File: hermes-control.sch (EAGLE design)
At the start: 71 parts, among them J3 2201778-1, Q1 MMBT2222A, Q2 BC849SMD, Q3 FDN360P, Q4 FDN360P, Q5 BC849SMD, Q6 MMBT2222A, Q7 FDN360P, U1 LSM9DS1TR, U2 ESP32-WROOM-32D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

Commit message: addressed more reviews
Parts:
- C15: value 100uF -> 100nF
- C9: value 10uF -> 10nF 16v
- R7: value 100k -> 100k 1%
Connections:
- removed net N$15: R6.1, U$2.2
- removed net N$16: C13.1, U1.VDDIO
- new net PROBE: R6.1, U$2.2, U2.IO33
- net 3.3V: now also C13.1, U1.VDDIO
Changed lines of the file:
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@@
 <part name="R20" library="rcl" library_urn="urn:adsk.eagle:library:334" deviceset="R-US_" device="R0603" package3d_urn="urn:adsk.eagle:package:23555/3" value="10k"/>
 <part name="R23" library="rcl" library_urn="urn:adsk.eagle:library:334" deviceset="R-US_" device="R0603" package3d_urn="urn:adsk.eagle:package:23555/3" value="33k"/>
-<part name="R7" library="rcl" library_urn="urn:adsk.eagle:library:334" deviceset="R-US_" device="R0603" package3d_urn="urn:adsk.eagle:package:23555/3" value="100k"/>
+<part name="R7" library="rcl" library_urn="urn:adsk.eagle:library:334" deviceset="R-US_" device="R0603" package3d_urn="urn:adsk.eagle:package:23555/3" value="100k 1%"/>
 <part name="R8" library="rcl" library_urn="urn:adsk.eagle:library:334" deviceset="R-US_" device="R0603" package3d_urn="urn:adsk.eagle:package:23555/3" value="10k"/>
 <part name="R9" library="rcl" library_urn="urn:adsk.eagle:library:334" deviceset="R-US_" device="R0603" package3d_urn="urn:adsk.eagle:package:23555/3" value="10k"/>
@@
 <part name="SUPPLY27" library="SparkFun-PowerSymbols" library_urn="urn:adsk.eagle:library:530" deviceset="VCC" device=""/>
 <part name="SUPPLY28" library="SparkFun-PowerSymbols" library_urn="urn:adsk.eagle:library:530" deviceset="3.3V" device=""/>
-<part name="C9" library="rcl" library_urn="urn:adsk.eagle:library:334" deviceset="C-US" device="C0603" package3d_urn="urn:adsk.eagle:package:23616/2" value="10uF"/>
-<part name="C15" library="rcl" library_urn="urn:adsk.eagle:library:334" deviceset="C-US" device="C0603" package3d_urn="urn:adsk.eagle:package:23616/2" value="100uF"/>
+<part name="C9" library="rcl" library_urn="urn:adsk.eagle:library:334" deviceset="C-US" device="C0603" package3d_urn="urn:adsk.eagle:package:23616/2" value="10nF 16v"/>
+<part name="C15" library="rcl" library_urn="urn:adsk.eagle:library:334" deviceset="C-US" device="C0603" package3d_urn="urn:adsk.eagle:package:23616/2" value="100nF"/>
 <part name="R4" library="rcl" library_urn="urn:adsk.eagle:library:334" deviceset="R-US_" device="R0603" package3d_urn="urn:adsk.eagle:package:23555/3" value="1k"/>
 <part name="R16" library="rcl" library_urn="urn:adsk.eagle:library:334" deviceset="R-US_" device="R0603" package3d_urn="urn:adsk.eagle:package:23555/3" value="1k"/>
@@
 <attribute name="VALUE" x="111.76" y="53.34" size="1.778" layer="96"/>
 </instance>
-<instance part="U$2" gate="G$1" x="83.82" y="83.82" smashed="yes" rot="R180"/>
-<instance part="GND29" gate="1" x="88.9" y="68.58" smashed="yes">
-<attribute name="VALUE" x="86.36" y="66.04" size="1.778" layer="96"/>
-</instance>
-<instance part="SUPPLY27" gate="G$1" x="88.9" y="86.36" smashed="yes">
-<attribute name="VALUE" x="88.9" y="89.154" size="1.778" layer="96" align="bottom-center"/>
+<instance part="U$2" gate="G$1" x="81.28" y="83.82" smashed="yes" rot="R180"/>
+<instance part="GND29" gate="1" x="86.36" y="68.58" smashed="yes">
+<attribute name="VALUE" x="83.82" y="66.04" size="1.778" layer="96"/>
+</instance>
+<instance part="SUPPLY27" gate="G$1" x="86.36" y="86.36" smashed="yes">
+<attribute name="VALUE" x="86.36" y="89.154" size="1.778" layer="96" align="bottom-center"/>
 </instance>
 <instance part="SUPPLY28" gate="G$1" x="200.66" y="134.62" smashed="yes">
@@
 <pinref part="GND29" gate="1" pin="GND"/>
 <pinref part="U$2" gate="G$1" pin="3"/>
-<wire x1="88.9" y1="71.12" x2="88.9" y2="76.2" width="0.1524" layer="91"/>
+<wire x1="86.36" y1="71.12" x2="86.36" y2="76.2" width="0.1524" layer="91"/>
 </segment>
 </net>
@@
 <pinref part="U$2" gate="G$1" pin="1"/>
 <pinref part="SUPPLY27" gate="G$1" pin="VCC"/>
-<wire x1="88.9" y1="81.28" x2="88.9" y2="86.36" width="0.1524" layer="91"/>
+<wire x1="86.36" y1="81.28" x2="86.36" y2="86.36" width="0.1524" layer="91"/>
 </segment>
 </net>
@@
 <pinref part="U1" gate="G$1" pin="VDD"/>
 <wire x1="411.48" y1="142.24" x2="414.02" y2="142.24" width="0.1524" layer="91"/>
-<wire x1="414.02" y1="142.24" x2="414.02" y2="160.02" width="0.1524" layer="91"/>
+<wire x1="414.02" y1="142.24" x2="414.02" y2="144.78" width="0.1524" layer="91"/>
+<wire x1="414.02" y1="144.78" x2="414.02" y2="160.02" width="0.1524" layer="91"/>
 <wire x1="391.16" y1="160.02" x2="403.86" y2="160.02" width="0.1524" layer="91"/>
 <pinref part="SUPPLY24" gate="G$1" pin="3.3V"/>
@@
 <pinref part="C12" gate="G$1" pin="1"/>
 <junction x="403.86" y="160.02"/>
+<pinref part="U1" gate="G$1" pin="VDDIO"/>
+<wire x1="411.48" y1="139.7" x2="419.1" y2="139.7" width="0.1524" layer="91"/>
+<wire x1="419.1" y1="139.7" x2="419.1" y2="144.78" width="0.1524" layer="91"/>
+<wire x1="419.1" y1="144.78" x2="426.72" y2="144.78" width="0.1524" layer="91"/>
+<pinref part="C13" gate="G$1" pin="1"/>
+<wire x1="419.1" y1="144.78" x2="414.02" y2="144.78" width="0.1524" layer="91"/>
+<junction x="419.1" y="144.78"/>
+<junction x="414.02" y="144.78"/>
 </segment>
 <segment>
@@
 </segment>
 </net>
-<net name="N$16" class="0">
-<segment>
-<pinref part="U1" gate="G$1" pin="VDDIO"/>
-<wire x1="411.48" y1="139.7" x2="419.1" y2="139.7" width="0.1524" layer="91"/>
-<wire x1="419.1" y1="139.7" x2="419.1" y2="144.78" width="0.1524" layer="91"/>
-<wire x1="419.1" y1="144.78" x2="426.72" y2="144.78" width="0.1524" layer="91"/>
-<pinref part="C13" gate="G$1" pin="1"/>
-</segment>
-</net>
 <net name="DTR" class="0">
 <segment>
@@
 <pinref part="Q6" gate="&gt;NAME" pin="C"/>
 <wire x1="114.3" y1="86.36" x2="114.3" y2="83.82" width="0.1524" layer="91"/>
-</segment>
-</net>
-<net name="N$15" class="0">
-<segment>
-<pinref part="U$2" gate="G$1" pin="2"/>
-<pinref part="R6" gate="G$1" pin="1"/>
-<wire x1="88.9" y1="78.74" x2="93.98" y2="78.74" width="0.1524" layer="91"/>
 </segment>
 </net>
@@
 </segment>
 </net>
+<net name="PROBE" class="0">
+<segment>
+<pinref part="U2" gate="G$1" pin="IO33"/>
+<wire x1="312.42" y1="88.9" x2="320.04" y2="88.9" width="0.1524" layer="91"/>
+<label x="314.96" y="88.9" size="1.778" layer="95"/>
+</segment>
+<segment>
+<pinref part="U$2" gate="G$1" pin="2"/>
+<pinref part="R6" gate="G$1" pin="1"/>
+<wire x1="86.36" y1="78.74" x2="93.98" y2="78.74" width="0.1524" layer="91"/>
+<label x="86.36" y="78.74" size="1.778" layer="95"/>
+</segment>
+</net>

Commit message: added two more i2c connections
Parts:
- removed U$6: JST-GH-4TOP, BlueRobotics-JST-GH:JST-GH-4TOP
- added U$10, U$11, U$9: JST-GH-4TOP, BlueRobotics-JST-GH:JST-GH-4TOP
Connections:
- net 3.3V: now also Q7.D, U$10.1, U$11.1, U$9.1; no longer Q7.S, U$6.1
- net GND: now also U$10.4, U$11.4, U$9.4; no longer U$6.4
- net SCL: now also U$10.2, U$11.2, U$9.2; no longer U$6.2
- net SDA: now also U$10.3, U$11.3, U$9.3; no longer U$6.3
- net VCCIO: now also Q7.S; no longer Q7.D
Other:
- moved on the sheet: Q7

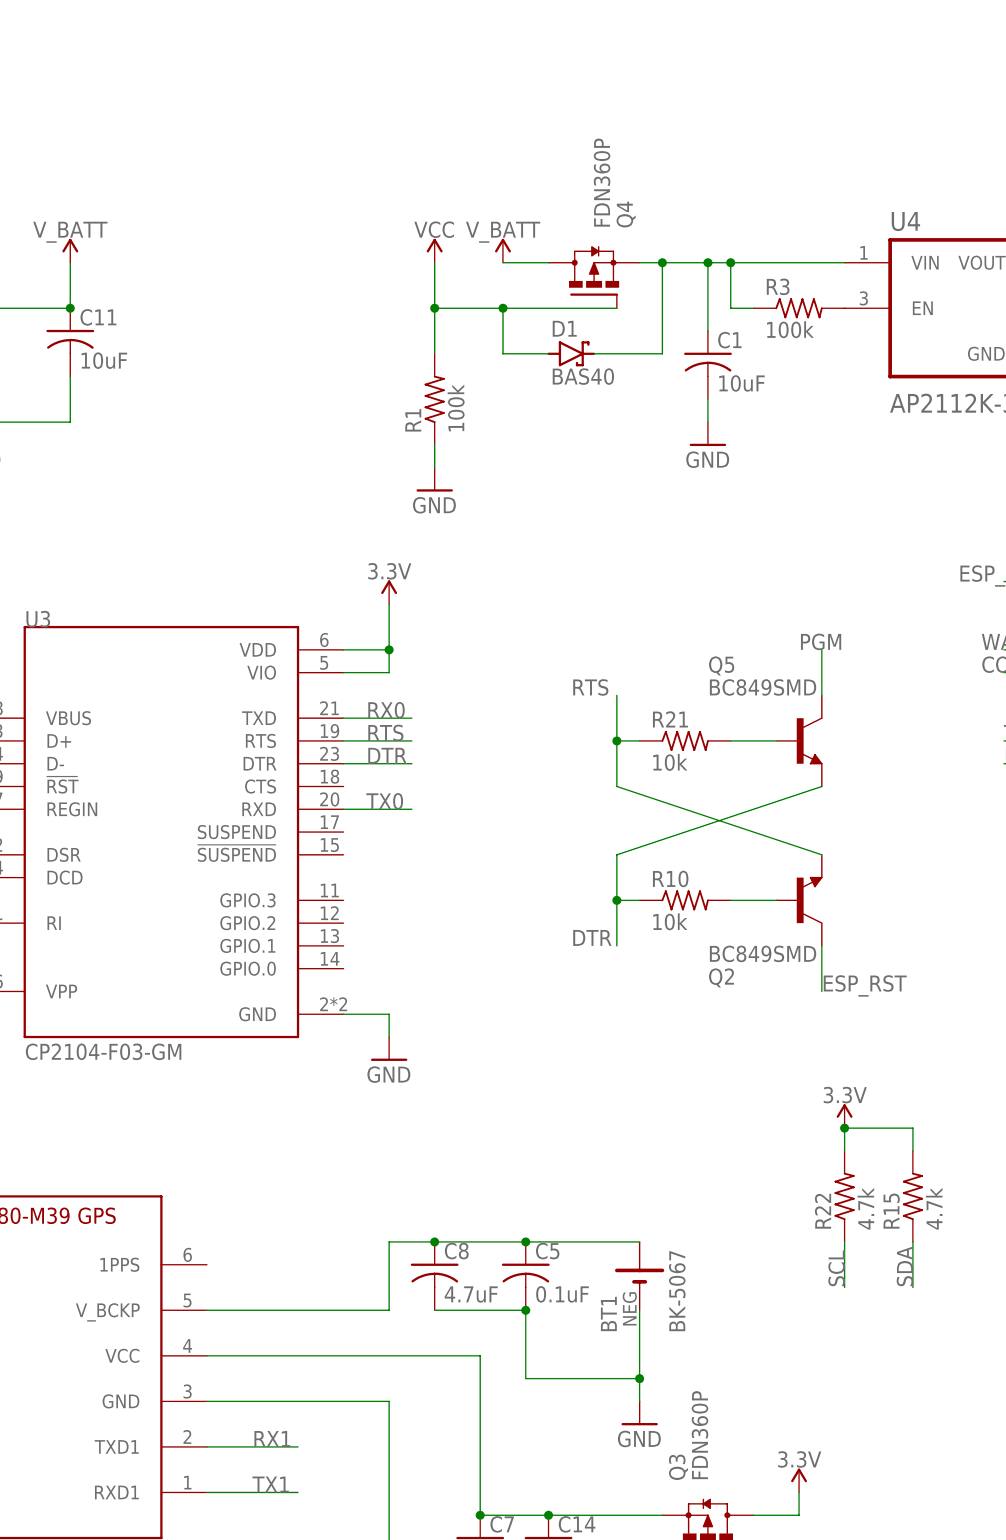
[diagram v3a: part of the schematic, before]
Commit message: new layout with main componets
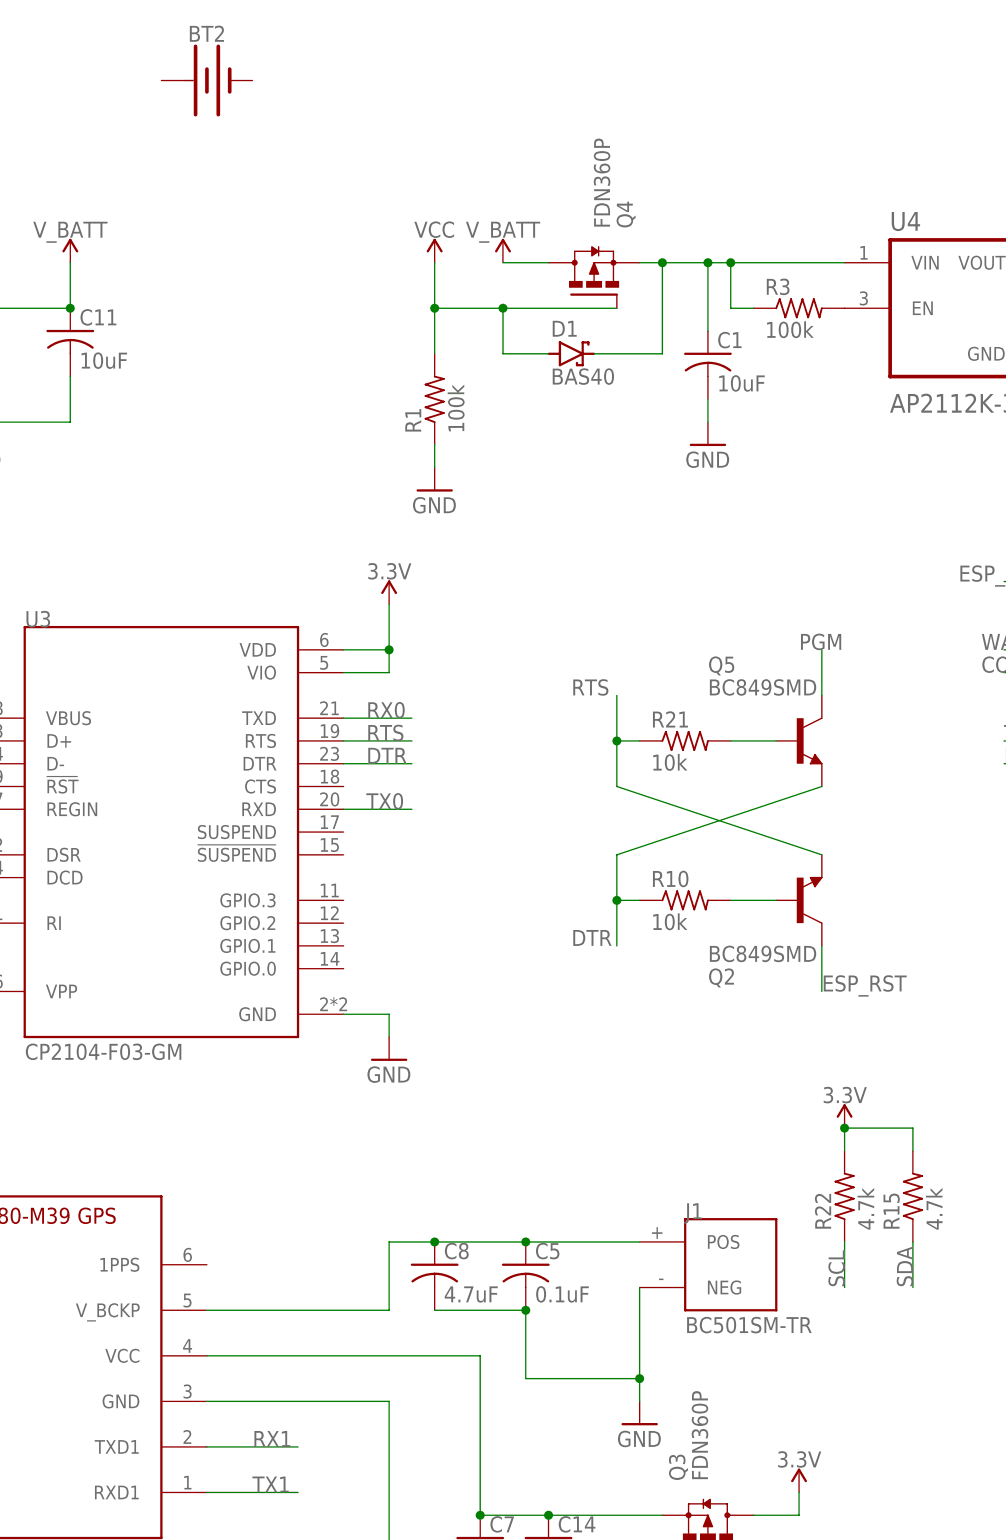
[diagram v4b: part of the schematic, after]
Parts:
- removed BT1: BK-5067, hermes:BK-5067
- added BT2: (no value), SparkFun-Batteries:BATTERY-18650
- added J1: BC501SM-TR, BC501SM-TR:BC501SM-TR
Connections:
- net GND: now also J1.NEG; no longer BT1.N
- net N$7: now also J1.POS; no longer BT1.P
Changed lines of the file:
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@@
 <?xml version="1.0" encoding="utf-8"?>
 <!DOCTYPE eagle SYSTEM "eagle.dtd">
-<eagle version="9.1.0">
+<eagle version="9.4.0">
 <drawing>
 <settings>
-<setting alwaysvectorfont="yes"/>
+<setting alwaysvectorfont="no"/>
 <setting verticaltext="up"/>
 </settings>
@@
 <part name="SUPPLY13" library="SparkFun-PowerSymbols" library_urn="urn:adsk.eagle:library:530" deviceset="V_BATT" device=""/>
 <part name="GND14" library="supply1" library_urn="urn:adsk.eagle:library:371" deviceset="GND" device=""/>
-<part name="S1" library="hermes" deviceset="1825910-7" device=""/>
 <part name="SUPPLY14" library="SparkFun-PowerSymbols" library_urn="urn:adsk.eagle:library:530" deviceset="3.3V" device=""/>
 <part name="GND15" library="supply1" library_urn="urn:adsk.eagle:library:371" deviceset="GND" device=""/>
@@
 <part name="GND13" library="supply1" library_urn="urn:adsk.eagle:library:371" deviceset="GND" device=""/>
 <part name="LBAT" library="hermes" deviceset="S2B-PH-SM4-TB(LF)(SN)" device=""/>
-<part name="BT1" library="hermes" deviceset="BK-5067" device=""/>
 <part name="S2" library="hermes" deviceset="1825910-7" device=""/>
 <part name="SUPPLY22" library="SparkFun-PowerSymbols" library_urn="urn:adsk.eagle:library:530" deviceset="3.3V" device=""/>
@@
 <part name="SUPPLY25" library="SparkFun-PowerSymbols" library_urn="urn:adsk.eagle:library:530" deviceset="3.3V" device=""/>
 <part name="SUPPLY29" library="SparkFun-PowerSymbols" library_urn="urn:adsk.eagle:library:530" deviceset="3.3V" device=""/>
+<part name="BT2" library="SparkFun-Batteries" library_urn="urn:adsk.eagle:library:508" deviceset="BATTERY" device="-18650" package3d_urn="urn:adsk.eagle:package:37227/1"/>
+<part name="J1" library="BC501SM-TR" deviceset="BC501SM-TR" device=""/>
+<part name="S1" library="hermes" deviceset="1825910-7" device=""/>
 </parts>
 <sheets>
@@
 <attribute name="VALUE" x="335.28" y="68.58" size="1.778" layer="96"/>
 </instance>
-<instance part="S1" gate="G$1" x="403.86" y="73.66" smashed="yes">
-<attribute name="NAME" x="403.86" y="75.184" size="1.778" layer="95" font="vector" align="bottom-center"/>
-</instance>
 <instance part="SUPPLY14" gate="G$1" x="421.64" y="66.04" smashed="yes">
 <attribute name="VALUE" x="421.64" y="68.834" size="1.778" layer="96" align="bottom-center"/>
@@
 <attribute name="VALUE" x="60.22268125" y="167.63188125" size="1.275409375" layer="96" rot="R90"/>
 </instance>
-<instance part="BT1" gate="G$1" x="228.6" y="60.96" smashed="yes" rot="R90">
-<attribute name="NAME" x="226.05975" y="53.33963125" size="1.778090625" layer="95" rot="R90"/>
-<attribute name="VALUE" x="233.68596875" y="53.331040625" size="1.780090625" layer="96" rot="R90"/>
-</instance>
 <instance part="S2" gate="G$1" x="403.86" y="58.42" smashed="yes">
 <attribute name="NAME" x="403.86" y="59.944" size="1.778" layer="95" font="vector" align="bottom-center"/>
@@
 <instance part="SUPPLY29" gate="G$1" x="43.18" y="104.14" smashed="yes">
 <attribute name="VALUE" x="43.18" y="106.934" size="1.778" layer="96" align="bottom-center"/>
+</instance>
+<instance part="BT2" gate="G$1" x="180.34" y="193.04" smashed="yes">
+<attribute name="NAME" x="180.34" y="197.358" size="1.778" layer="95" font="vector" align="bottom-center"/>
+<attribute name="VALUE" x="180.34" y="188.722" size="1.778" layer="96" font="vector" align="top-center"/>
+</instance>
+<instance part="J1" gate="G$1" x="238.76" y="60.96" smashed="yes">
+<attribute name="NAME" x="233.68" y="66.04" size="1.778" layer="95"/>
+<attribute name="VALUE" x="233.68" y="53.34" size="1.778" layer="96"/>
+</instance>
+<instance part="S1" gate="G$1" x="403.86" y="73.66" smashed="yes">
+<attribute name="NAME" x="403.86" y="75.184" size="1.778" layer="95" font="vector" align="bottom-center"/>
 </instance>
 </instances>
@@
 <pinref part="GND9" gate="1" pin="GND"/>
 <wire x1="228.6" y1="45.72" x2="228.6" y2="48.26" width="0.1524" layer="91"/>
-<wire x1="228.6" y1="48.26" x2="228.6" y2="55.88" width="0.1524" layer="91"/>
+<wire x1="228.6" y1="48.26" x2="228.6" y2="58.42" width="0.1524" layer="91"/>
 <wire x1="215.9" y1="55.88" x2="215.9" y2="48.26" width="0.1524" layer="91"/>
 <wire x1="215.9" y1="48.26" x2="228.6" y2="48.26" width="0.1524" layer="91"/>
 <junction x="228.6" y="48.26"/>
 <wire x1="205.74" y1="55.88" x2="215.9" y2="55.88" width="0.1524" layer="91"/>
-<pinref part="BT1" gate="G$1" pin="N"/>
 <pinref part="C5" gate="G$1" pin="2"/>
 <junction x="215.9" y="55.88"/>
 <pinref part="C8" gate="G$1" pin="2"/>
+<pinref part="J1" gate="G$1" pin="NEG"/>
 </segment>
 <segment>
@@
 <wire x1="421.64" y1="66.04" x2="416.56" y2="66.04" width="0.1524" layer="91"/>
 <wire x1="416.56" y1="66.04" x2="416.56" y2="71.12" width="0.1524" layer="91"/>
-<pinref part="S1" gate="G$1" pin="4"/>
 <wire x1="416.56" y1="71.12" x2="414.02" y2="71.12" width="0.1524" layer="91"/>
 <wire x1="416.56" y1="66.04" x2="416.56" y2="60.96" width="0.1524" layer="91"/>
@@
 <pinref part="S2" gate="G$1" pin="3"/>
 <wire x1="416.56" y1="60.96" x2="414.02" y2="60.96" width="0.1524" layer="91"/>
+<pinref part="S1" gate="G$1" pin="4"/>
 </segment>
 <segment>
@@
 <pinref part="U$1" gate="G$1" pin="V_BCKP"/>
 <wire x1="200.66" y1="55.88" x2="180.34" y2="55.88" width="0.1524" layer="91"/>
-<pinref part="BT1" gate="G$1" pin="P"/>
 <pinref part="C5" gate="G$1" pin="1"/>
 <junction x="215.9" y="63.5"/>
 <pinref part="C8" gate="G$1" pin="1"/>
 <junction x="205.74" y="63.5"/>
+<pinref part="J1" gate="G$1" pin="POS"/>
 </segment>
 </net>
@@
 <net name="CONFIG" class="0">
 <segment>
-<pinref part="S1" gate="G$1" pin="1"/>
 <wire x1="393.7" y1="76.2" x2="386.08" y2="76.2" width="0.1524" layer="91"/>
 <label x="383.54" y="76.2" size="1.778" layer="95"/>
 <pinref part="R8" gate="G$1" pin="2"/>
-</segment>
-<segment>
+<pinref part="S1" gate="G$1" pin="1"/>
+</segment>
+<segment>

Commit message: all componets placed
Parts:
- removed J2: (no value), SparkFun-Connectors:USB_MICRO-B_FEMALE-SMT
- removed S3: 1825910-7, hermes:1825910-7
- added BT1: 6.8MM_COIN_CELL, SparkFun-Batteries:BATTERY-6.8MM_SMD
- added D2: BAS40, diode:BAS40
- added Q8: MMBT2222A, hermes:MMBT2222A
- added R19: 1k, rcl:R-US_R0603
- added R25: 4.7k, rcl:R-US_R0603
- J1: value BC501SM-TR -> 1981568-1; device BC501SM-TR:BC501SM-TR -> SnapEDA-Library (1):1981568-1
- Q6: value MMBT2222A -> MMBT3906SOT23-3; device hermes:MMBT2222A -> MMBT3906:MMBT3906SOT23-3
- R23: value 33k -> 33k 1%
- S1, S2: value 1825910-7 -> 1437566-4; device hermes:1825910-7 -> 1437566-4:1437566-4
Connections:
- net RL_33 renamed 3.3_EN
- removed net N$7: C5.1, C8.1, J1.POS, U$1.V_BCKP
- removed net USER: R9.2, S2.2, U2.IO35
- new net N$15: BT1.+, C5.1, C8.1, R19.1, U$1.V_BCKP
- new net N$16: D2.C, R19.2
- new net N$24: Q8.B, R25.1
- new net VCC_SENSE: Q8.E, R9.2, U2.IO35
- net 3.3V: now also D2.A, Q8.C, S2.2; no longer S1.4, S2.3
- net CONFIG: now also S2.1; no longer S1.1
- net D+: now also J1.3; no longer J2.D+
- net D-: now also J1.2; no longer J2.D-
- net ESP_RST: now also S1.1; no longer S3.1
- net GND: now also BT1.-, J1.5, J1.SHIELD, S1.2, U5.EP; no longer J1.NEG, J2.GND, S3.4
- net N$14: now also Q6.E; no longer Q6.C
- net VCC: now also J1.1, R25.2; no longer J2.VBUS
- net WATER: now also Q6.C; no longer Q6.E
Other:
- moved on the sheet: R9
